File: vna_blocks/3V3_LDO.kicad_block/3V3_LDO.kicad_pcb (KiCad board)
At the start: 4 copper layers, 7 parts, among them U11 LT3041ADE-PBF

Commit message: hmc7044 design block
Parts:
- removed C131, C136: 10u, Capacitor_SMD:C_0402_1005Metric
- removed C134: 4.7u, Capacitor_SMD:C_0603_1608Metric
- removed R44: 49.9k, Resistor_SMD:R_0402_1005Metric
- removed R45: 140k, Resistor_SMD:R_0402_1005Metric
- removed R46: 10k, Resistor_SMD:R_0402_1005Metric
- removed U11: LT3041ADE-PBF, VNA_fp:05-08-1708_ADI-L
- added C331: 10u, Capacitor_SMD:C_0402_1005Metric, B.Cu at (57.5, 328.8)
- added C337: 4.7u, Capacitor_SMD:C_0603_1608Metric, B.Cu at (50.0, 331.5)
- added C340: 10u, Capacitor_SMD:C_0402_1005Metric, B.Cu at (51.5, 328.7)
- added C341: 10u, Capacitor_SMD:C_0402_1005Metric, B.Cu at (50.6, 328.7)
- added R176: 33.2k, Resistor_SMD:R_0402_1005Metric, B.Cu at (51.5, 331.5)
- added R181: 89k, Resistor_SMD:R_0402_1005Metric, B.Cu at (51.7, 333.8)
- added R182: 10k, Resistor_SMD:R_0402_1005Metric, B.Cu at (53.7, 333.8)
- added U36: LT3041ADE-PBF, VNA_fp:05-08-1708_ADI-L, B.Cu at (54.2, 330.8)

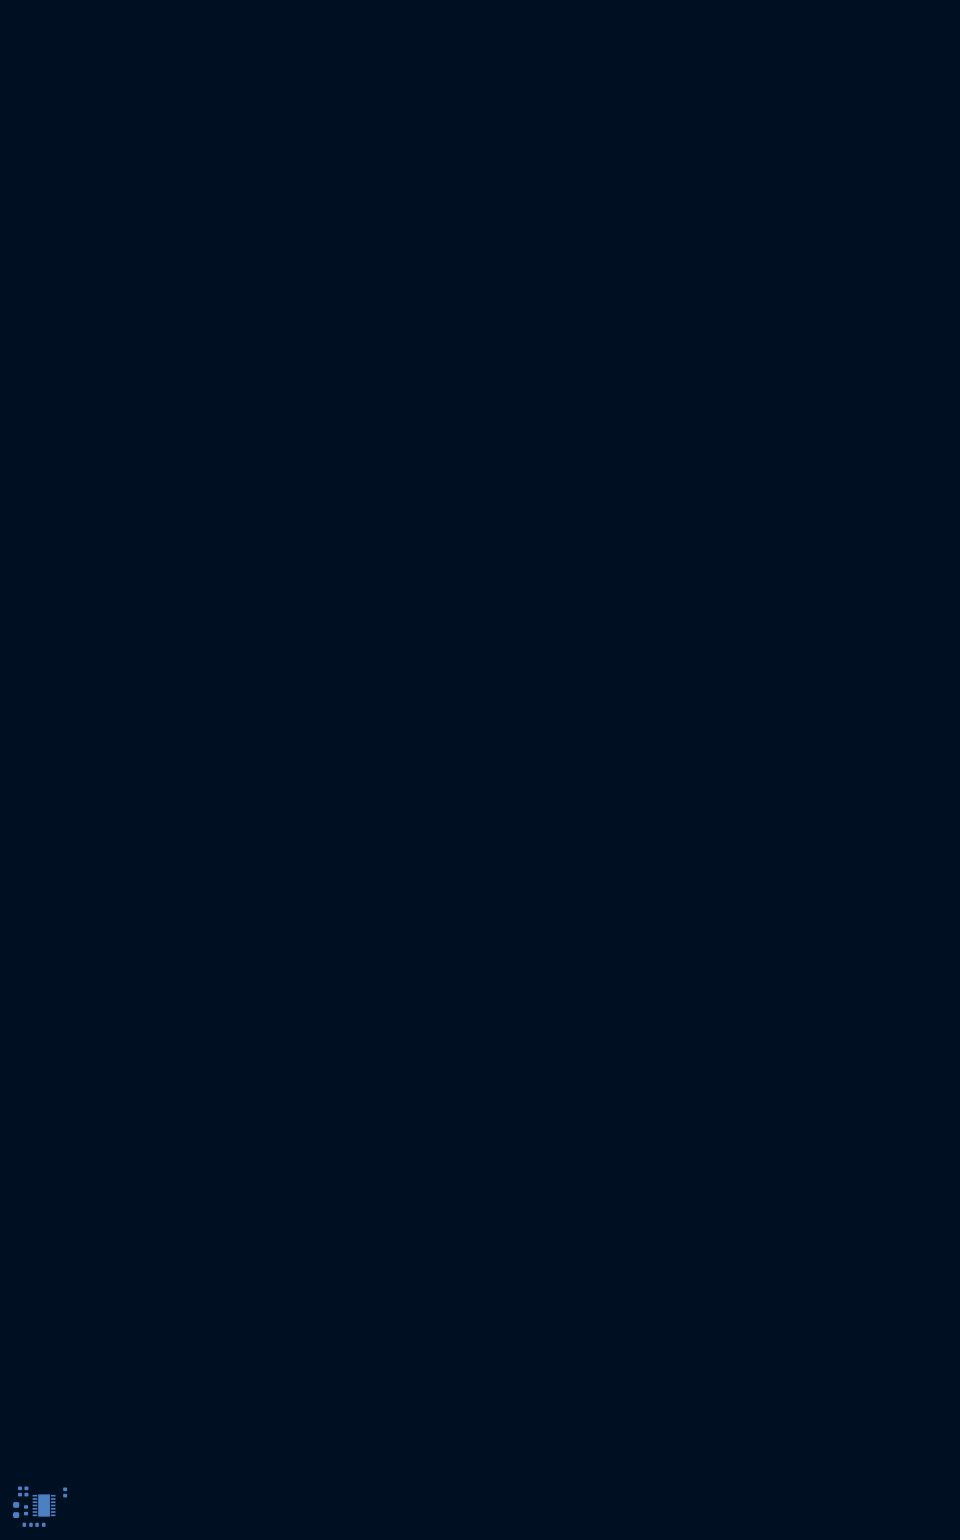
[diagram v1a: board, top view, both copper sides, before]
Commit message: fixed 50 ohm for coax port, fixed power blocks
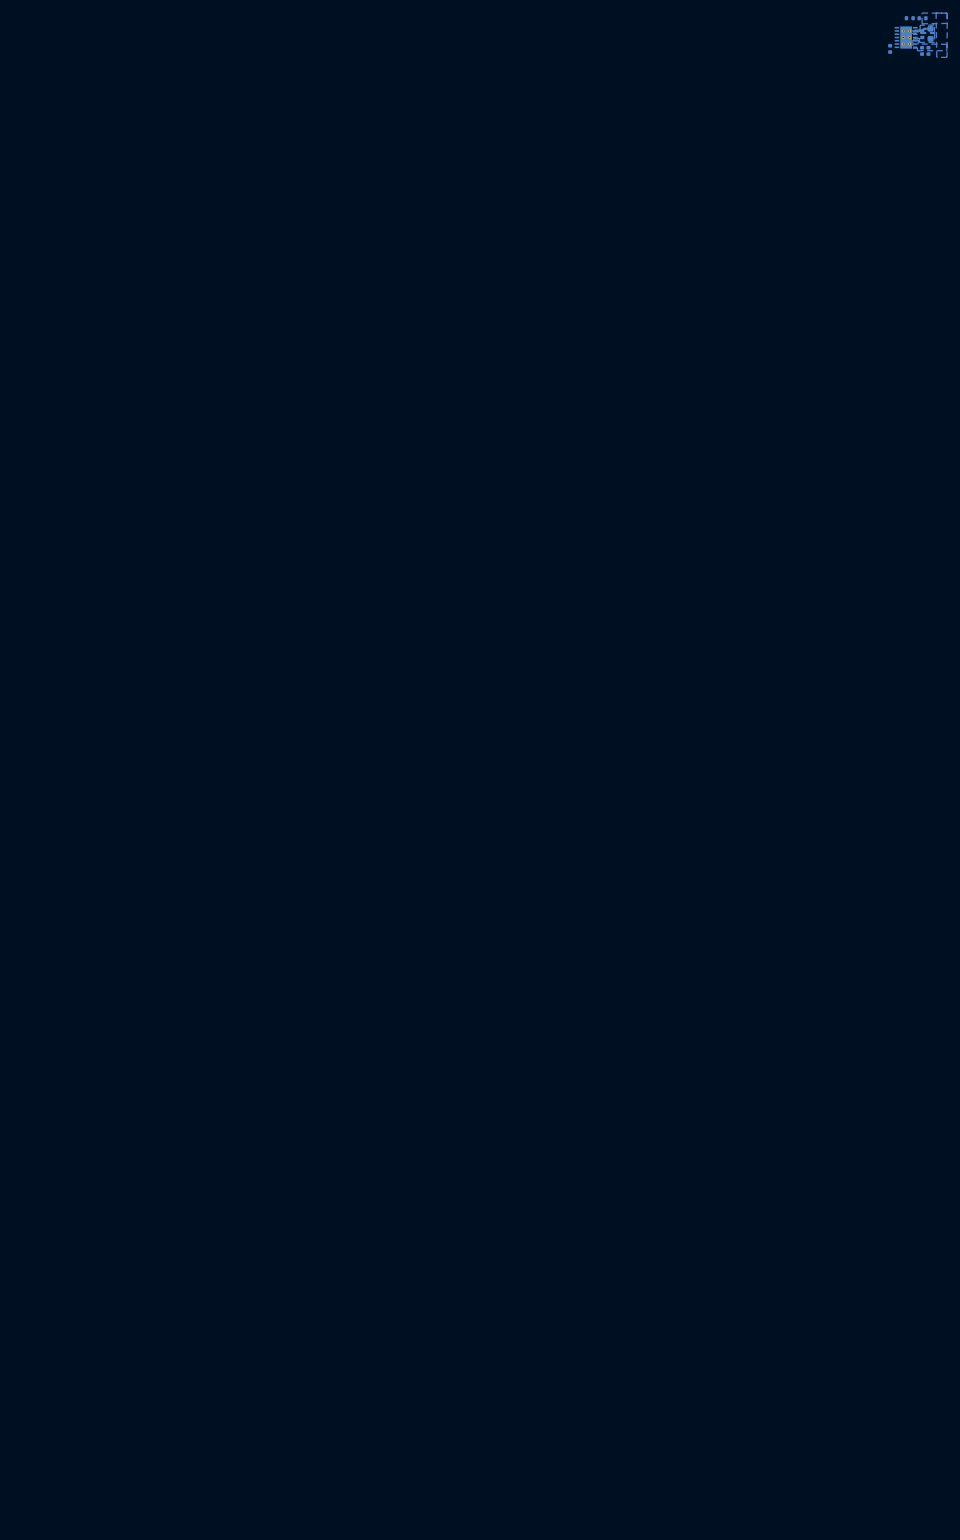
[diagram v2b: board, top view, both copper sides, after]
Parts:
- removed C331, C340, C341: 10u, Capacitor_SMD:C_0402_1005Metric
- removed C337: 4.7u, Capacitor_SMD:C_0603_1608Metric
- removed R176: 33.2k, Resistor_SMD:R_0402_1005Metric
- removed R181: 89k, Resistor_SMD:R_0402_1005Metric
- removed R182: 10k, Resistor_SMD:R_0402_1005Metric
- removed U36: LT3041ADE-PBF, VNA_fp:05-08-1708_ADI-L
- added C330: 10u, Capacitor_SMD:C_0402_1005Metric, B.Cu at (183.8, 107.8)
- added C334: 4.7u, Capacitor_SMD:C_0603_1608Metric, B.Cu at (190.0, 105.5)
- added C336: 10u, Capacitor_SMD:C_0402_1005Metric, B.Cu at (188.7, 108.1)
- added C339: 10u, Capacitor_SMD:C_0402_1005Metric, B.Cu at (189.6, 108.1)
- added R175: 33.2k, Resistor_SMD:R_0402_1005Metric, B.Cu at (188.7, 105.5)
- added R179: 89k, Resistor_SMD:R_0402_1005Metric, B.Cu at (188.7, 103.1)
- added R180: 10k, Resistor_SMD:R_0402_1005Metric, B.Cu at (186.8, 103.1)
- added U35: LT3041ADE-PBF, VNA_fp:05-08-1708_ADI-L, B.Cu at (186.2, 106.0)
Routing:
- net Net-(U35-SET): track 0.00 -> 2.49 mm
- added copper zone on B.Cu, net /3V3_Synth
- added copper zone on B.Cu, net GNDA
- added copper zone on B.Cu, net Net-(U35-SET)
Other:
- copper layers 4 -> 8
